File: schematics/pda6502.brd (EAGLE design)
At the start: 100 x 80 mm, 34 parts, among them IC1 74HC00D, IC2 74HC138D, IC3 DS1813-SMD, J1 CON_HEADER_2X07-PTH, U1 W65C02S, U2 W65C22S, U3 28C256, U4 UM61256AK-12

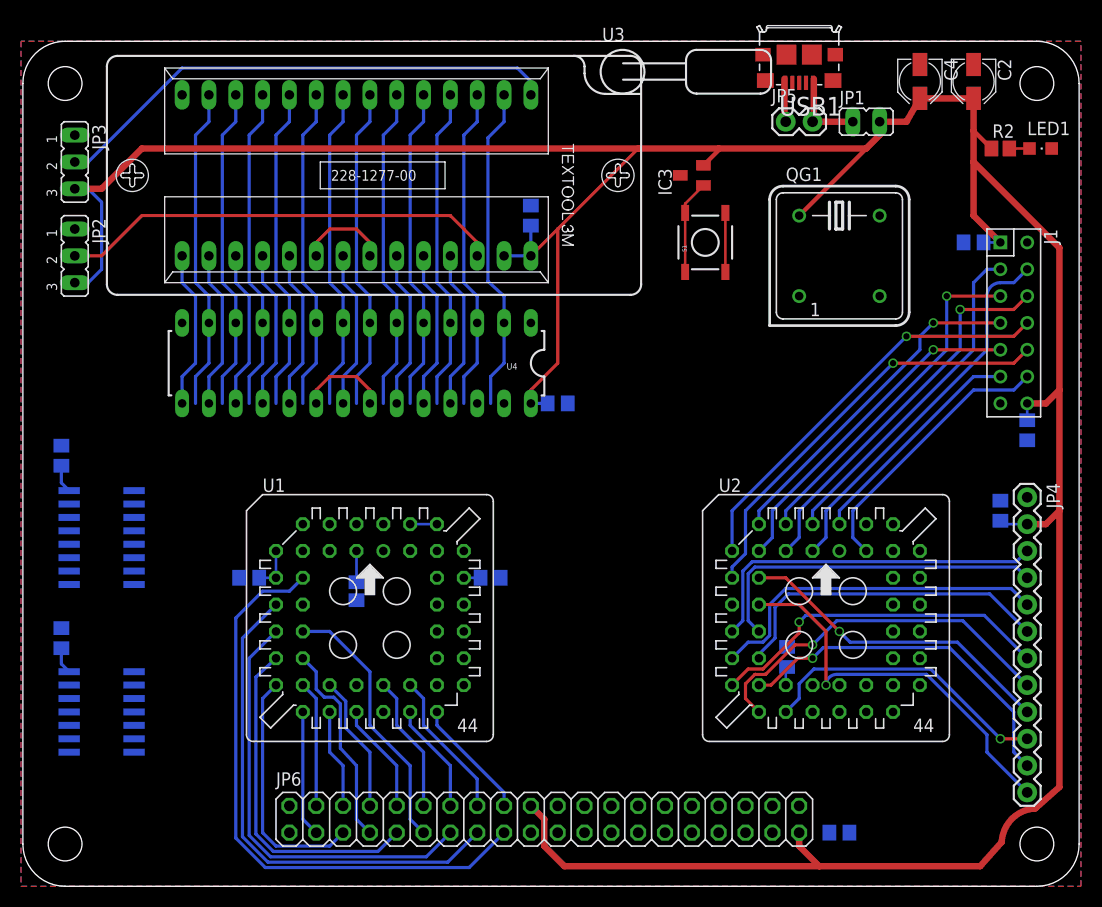
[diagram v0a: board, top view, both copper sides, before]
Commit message: board: re-routed expansion port address lines to 6502.
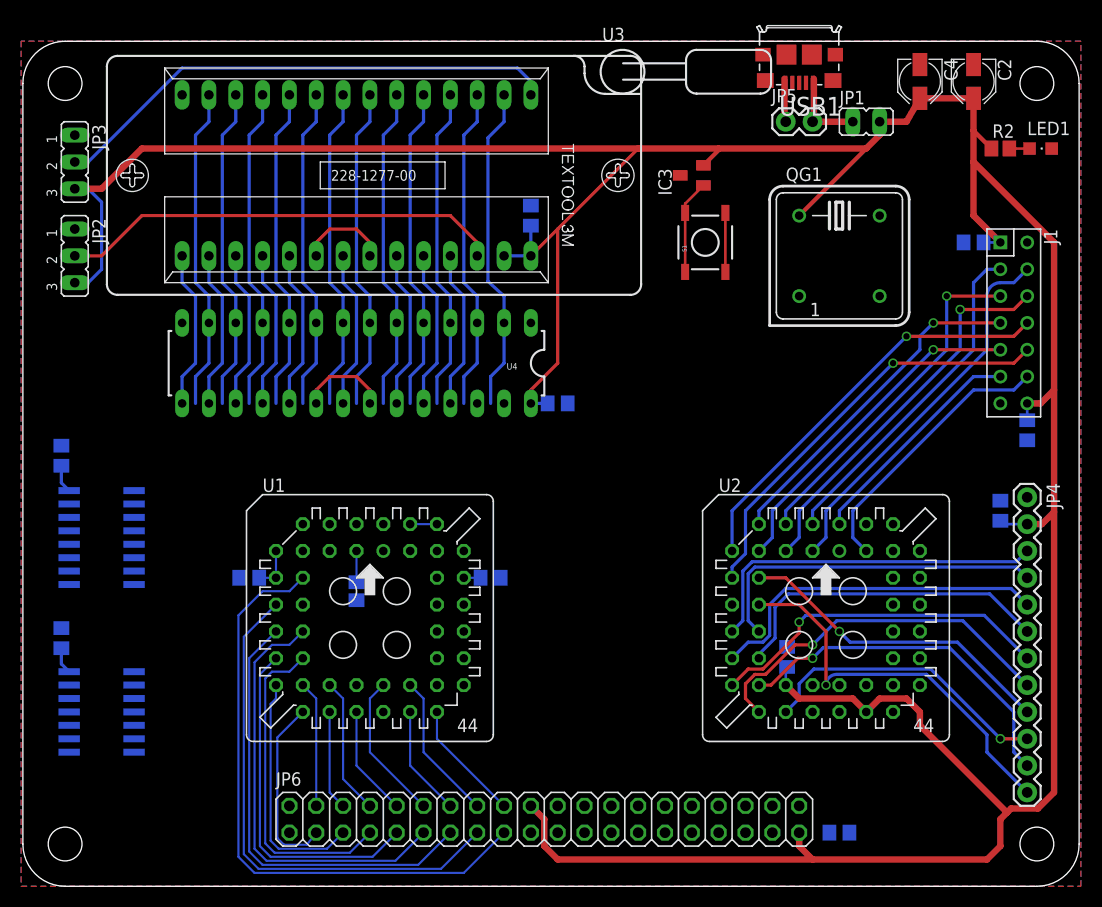
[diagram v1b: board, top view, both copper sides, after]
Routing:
- net 5V: track 321.5 -> 347.8 mm
- net ADDR3: track 56.1 -> 71.8 mm
- net ADDR5: track 50.4 -> 61.8 mm
- net ADDR7: track 42.7 -> 48.2 mm
- net ADDR2: track 72.0 -> 73.5 mm
- net ADDR1: track 78.5 -> 79.8 mm
- net ADDR0: track 87.5 -> 88.6 mm
- net ADDR12: track 44.0 -> 45.1 mm
- net ADDR4: track 63.0 -> 63.5 mm

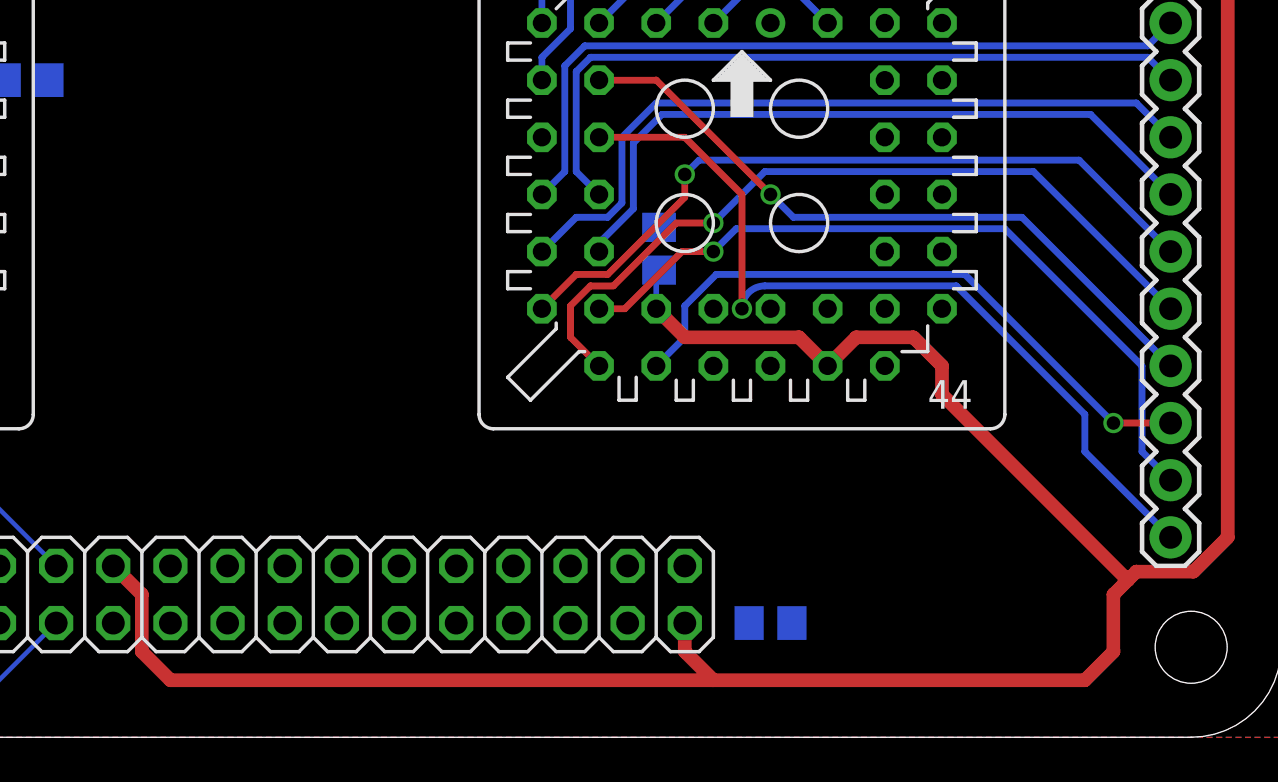
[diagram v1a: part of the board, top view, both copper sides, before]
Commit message: board: routed expansion port DATA to 6522.
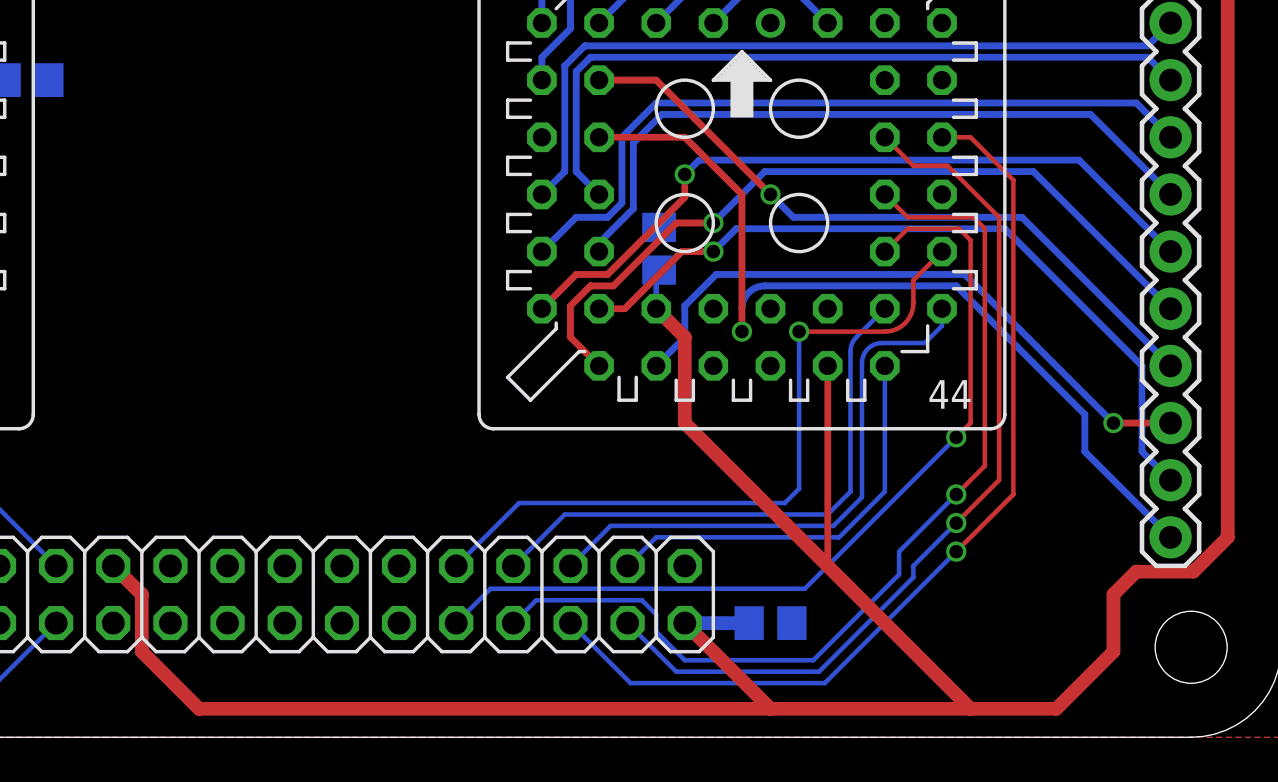
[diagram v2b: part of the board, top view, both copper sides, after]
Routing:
- net DATA2: track 30.8 -> 73.5 mm, vias 0 -> 1
- net DATA1: track 30.8 -> 73.0 mm, vias 0 -> 1
- net DATA0: track 30.8 -> 70.3 mm, vias 0 -> 1
- net DATA3: track 15.0 -> 54.1 mm, vias 0 -> 1
- net DATA4: track 15.0 -> 47.1 mm, vias 0 -> 1
- net DATA6: track 15.0 -> 40.2 mm
- net DATA5: track 15.0 -> 40.1 mm
- net DATA7: track 15.0 -> 33.4 mm
- net 5V: track 347.8 -> 358.8 mm
- net PB1: track 37.5 -> 39.6 mm

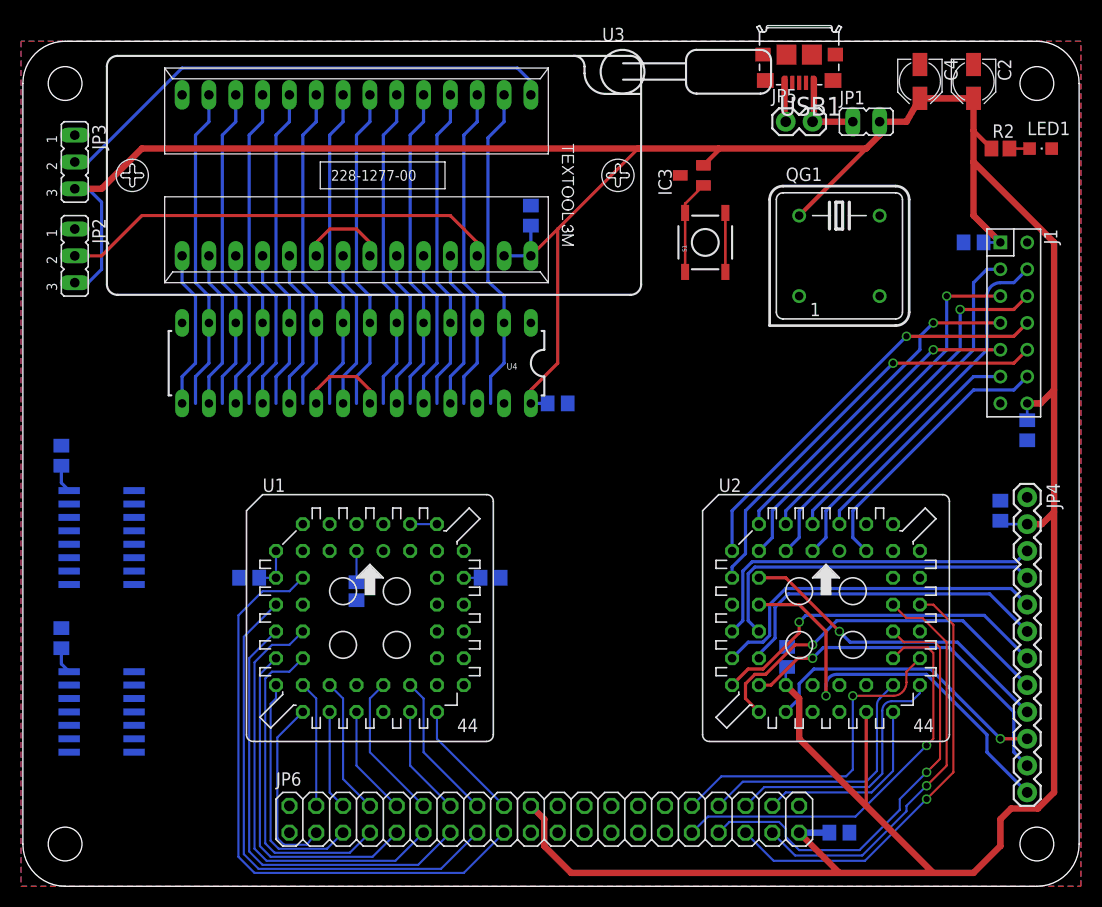
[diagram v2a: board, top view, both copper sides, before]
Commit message: board: further routing, placement adjustments.
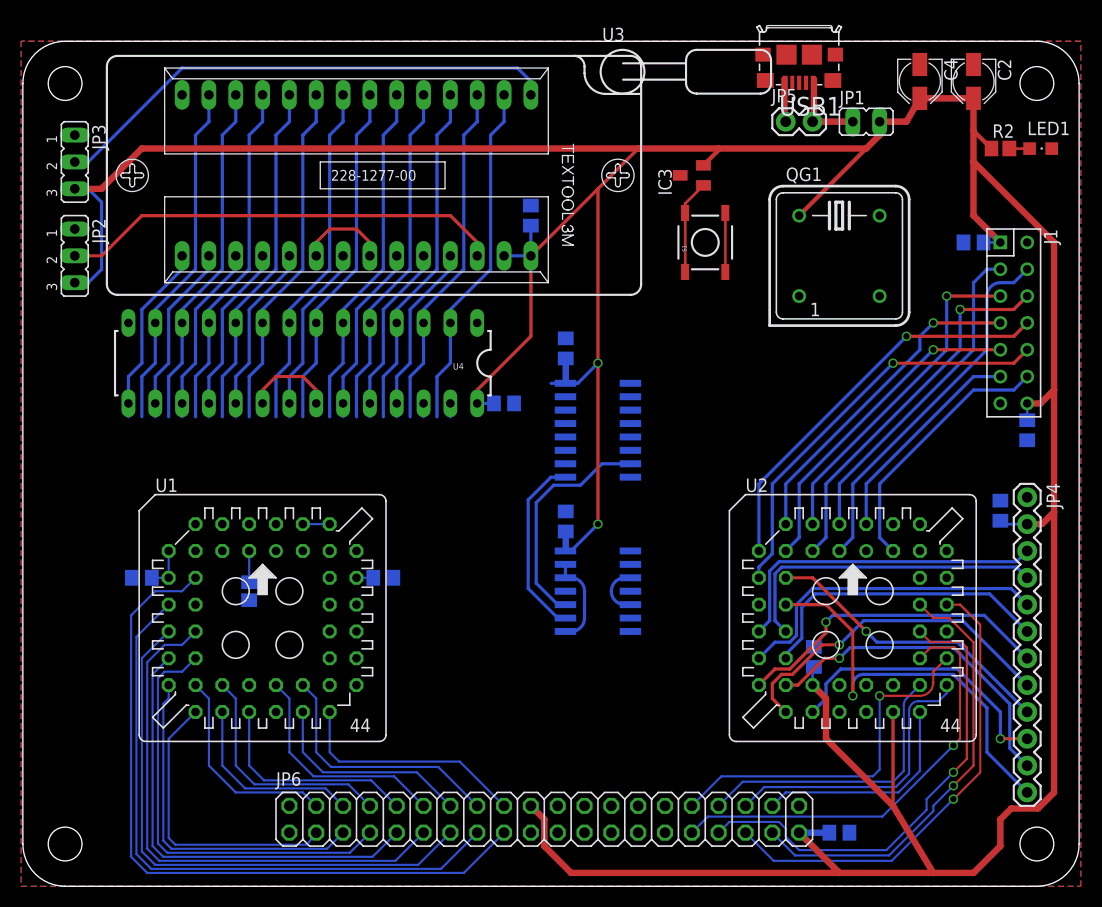
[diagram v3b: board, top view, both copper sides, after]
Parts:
- moved C6 49.0 mm to (51.6, 34.5)
- moved C7 48.8 mm to (51.6, 50.9)
- moved IC1 48.4 mm to (54.6, 27.9)
- moved IC2 48.1 mm to (54.6, 43.2)
- moved C3 10.2 mm to (34.3, 29.2)
- moved U1 10.2 mm to (22.9, 26.7)
- moved C1 10.2 mm to (11.4, 29.2)
- moved R1 10.2 mm to (21.6, 27.9)
- moved C10 5.08 mm to (45.7, 45.7)
- moved U4 5.08 mm to (26.7, 49.5)
- moved C5 2.54 mm to (75.1, 21.7)
- moved U2 2.54 mm to (78.7, 26.7)
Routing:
- net 5V: track 358.8 -> 395.8 mm, vias 0 -> 2
- net N$2: track 0.00 -> 21.7 mm
- net N$3: track 0.00 -> 18.0 mm
- net ADDR7: track 48.2 -> 60.9 mm
- net ADDR3: track 71.8 -> 84.3 mm
- net ADDR0: track 88.6 -> 101.1 mm
- net ADDR11: track 25.5 -> 38.0 mm
- net ADDR1: track 79.8 -> 92.3 mm
- net ADDR4: track 63.5 -> 76.0 mm
- net ADDR2: track 73.5 -> 86.0 mm
- net ADDR6: track 53.5 -> 66.0 mm
- net ADDR5: track 61.8 -> 74.3 mm
- net ADDR10: track 28.0 -> 39.8 mm
- net ADDR9: track 24.4 -> 35.4 mm
- net ADDR15: track 11.5 -> 22.4 mm
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
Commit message: board: routing fine-tuned around expansion port.
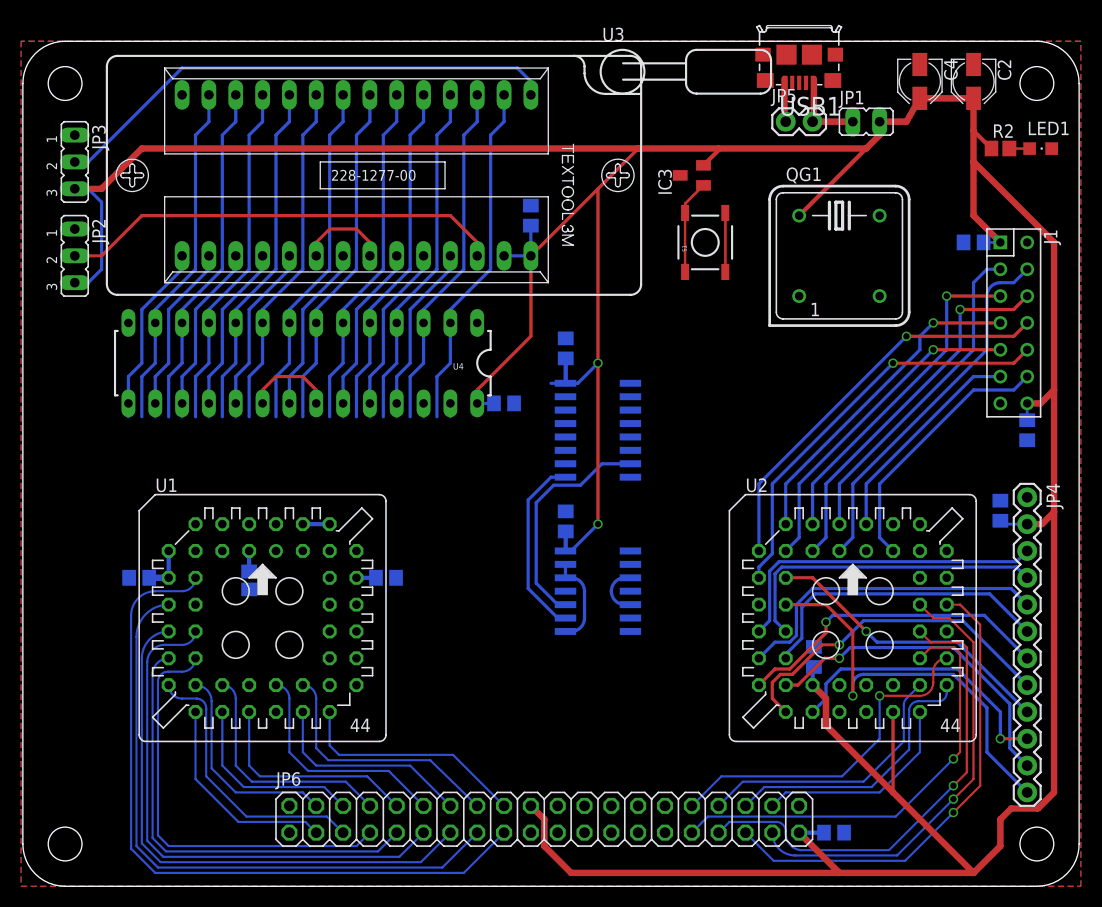
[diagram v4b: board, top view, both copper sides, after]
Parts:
- moved R1 1.02 mm to (21.6, 29.0)
- moved C13 0.51 mm to (77.0, 5.08)
- moved C1 0.25 mm to (11.2, 29.2)
- moved C3 0.25 mm to (34.5, 29.2)
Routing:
- net ADDR7: track 60.9 -> 53.0 mm
- net ADDR6: track 66.0 -> 59.2 mm
- net DATA4: track 51.9 -> 50.2 mm
- net DATA5: track 44.9 -> 43.3 mm
- net DATA6: track 45.1 -> 43.7 mm
- net ADDR5: track 74.3 -> 73.1 mm
- net DATA7: track 38.3 -> 37.2 mm
- net N$9: track 2.96 -> 1.94 mm
- net ADDR4: track 76.0 -> 75.1 mm
- net 5V: track 395.8 -> 396.7 mm
- net ADDR3: track 84.3 -> 83.5 mm
- net DATA3: track 59.0 -> 59.7 mm
- net DATA1: track 77.8 -> 78.6 mm
- net ADDR2: track 86.0 -> 85.3 mm
- net ADDR1: track 92.3 -> 91.7 mm

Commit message: board: PORTB bumped north; fine trace width normalized, tweaks.
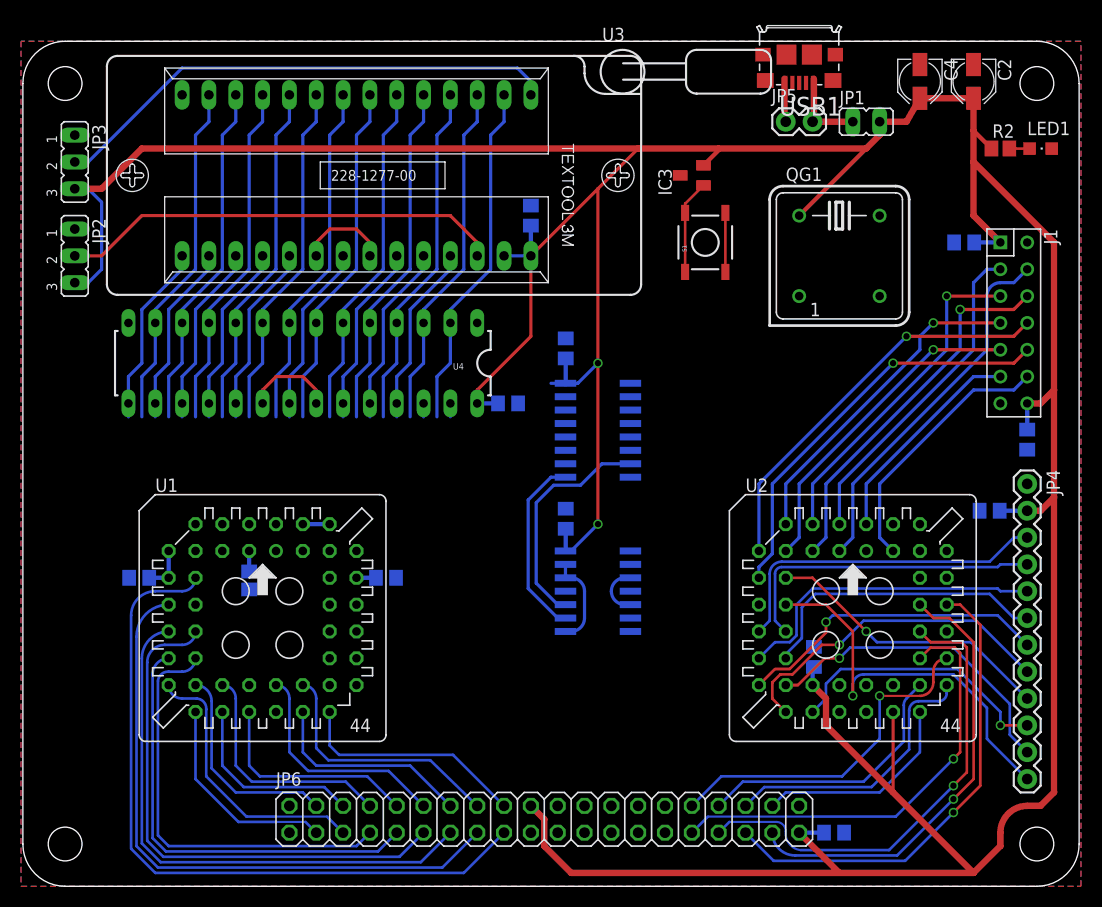
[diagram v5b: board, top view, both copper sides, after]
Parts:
- moved JP4 1.27 mm to (95.2, 38.1)
- moved C9 1.02 mm to (91.7, 35.6), turned to 0 degrees
- moved C12 0.89 mm to (95.2, 42.3)
- moved C11 0.89 mm to (89.3, 61.0)
- moved C10 0.38 mm to (46.1, 45.7)
- moved C6 0.25 mm to (51.6, 34.8)
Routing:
- net 5V: track 396.7 -> 398.3 mm
- net PB1: track 38.5 -> 37.3 mm
- net CB2: track 27.0 -> 25.8 mm
- net CB1: track 31.4 -> 30.1 mm
- net PB6: track 30.4 -> 29.9 mm
- net PB5: track 28.8 -> 28.3 mm
- net PB4: track 30.5 -> 30.0 mm
- net PB0: track 28.1 -> 27.6 mm
- net PB7: track 32.4 -> 31.9 mm
